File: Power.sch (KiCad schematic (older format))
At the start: 63 parts, among them J16 Power Input, J17 VS, J18 12V, J19 5V, J20 3.3V, Q8 YJS9435A, U6 MCP16301, U7 A4403, U8 MCP16301

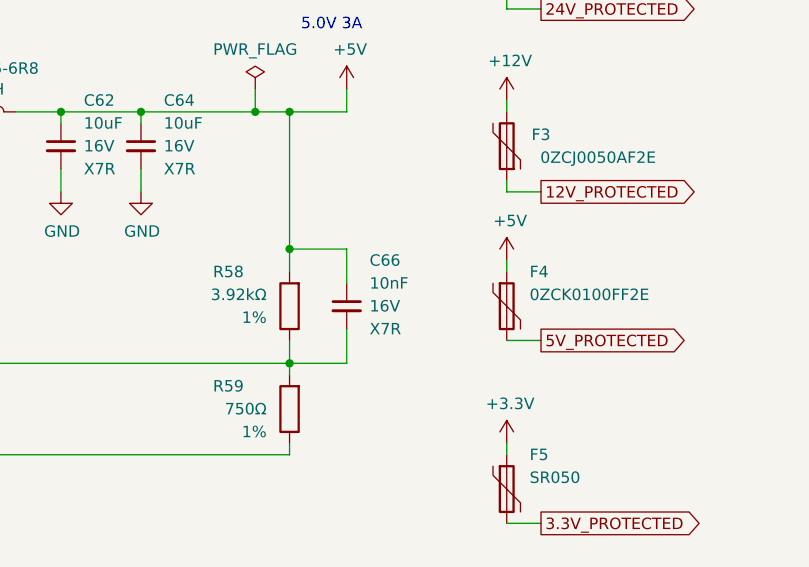
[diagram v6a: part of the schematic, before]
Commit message: Update elements value
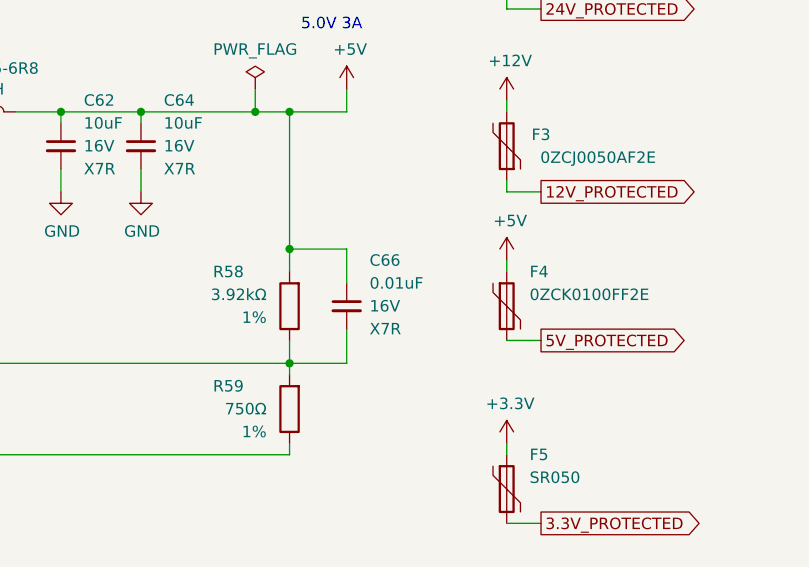
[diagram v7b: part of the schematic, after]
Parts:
- C66: value 10nF -> 0.01uF
- D24: Cena (none) -> 0.14862; Link (none) -> https://www.tme.eu/pl/details/mmsz5236bs-7-f/diody-zenera-s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; Model (none) -> MMSZ5236BS-7-F; Napięcie (none) -> 7.5V; Opis (none) -> Dioda: Zenera; 0,2W; 7,5V; SMD; rolka,taśma; SOD323; Producent (none) -> DIODES INCORPORATED; Typ (none) -> SMD
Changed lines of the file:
@@
 AR Path="/5E1018C2/5E102C60" Ref="C66"  Part="1"
 F 0 "C66" H 9000 3100 50  0000 L CNN
-F 1 "10nF" H 9000 3000 50  0000 L CNN
+F 1 "0.01uF" H 9000 3000 50  0000 L CNN
 F 2 "Capacitor_SMD:C_0603_1608Metric" H 8900 2900 50  0001 C CNN
 F 3 "~" H 8900 2900 50  0001 C CNN
@@
 F 2 "Diode_SMD:D_SOD-323" H 4750 6100 50  0001 C CNN
 F 3 "~" H 4750 6100 50  0001 C CNN
+F 4 "0.14862" H 4750 6100 50  0001 C CNN "Cena"
+F 5 "https://www.tme.eu/pl/details/mmsz5236bs-7-f/diody-zenera-smd/diodes-incorporated/" H 4750 6100 50  0001 C CNN "Link"
+F 6 "MMSZ5236BS-7-F" H 4750 6100 50  0001 C CNN "Model"
+F 7 "7.5V" H 4750 6100 50  0001 C CNN "Napięcie"
+F 8 "Dioda: Zenera; 0,2W; 7,5V; SMD; rolka,taśma; SOD323" H 4750 6100 50  0001 C CNN "Opis"
+F 9 "DIODES INCORPORATED" H 4750 6100 50  0001 C CNN "Producent"
+F 10 "SMD" H 4750 6100 50  0001 C CNN "Typ"
 	1    4750 6100
 	0    -1   -1   0

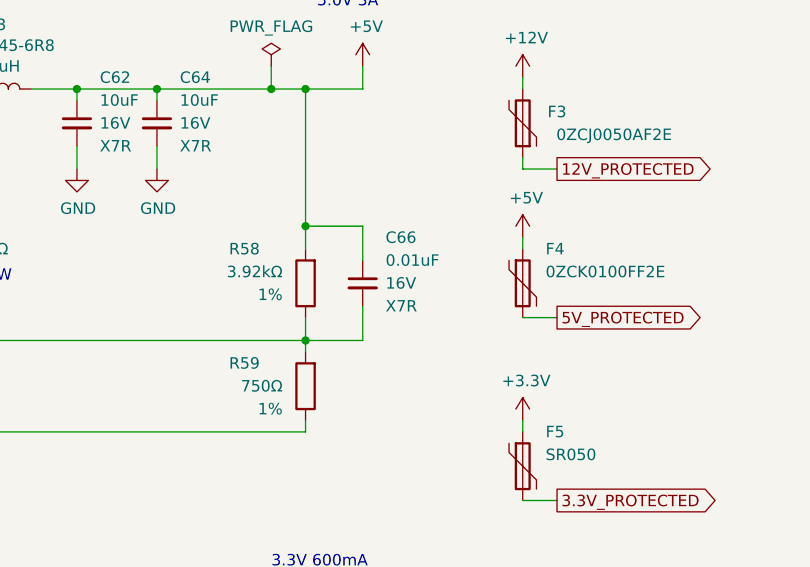
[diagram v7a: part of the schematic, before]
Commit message: Updated BOM on schematics
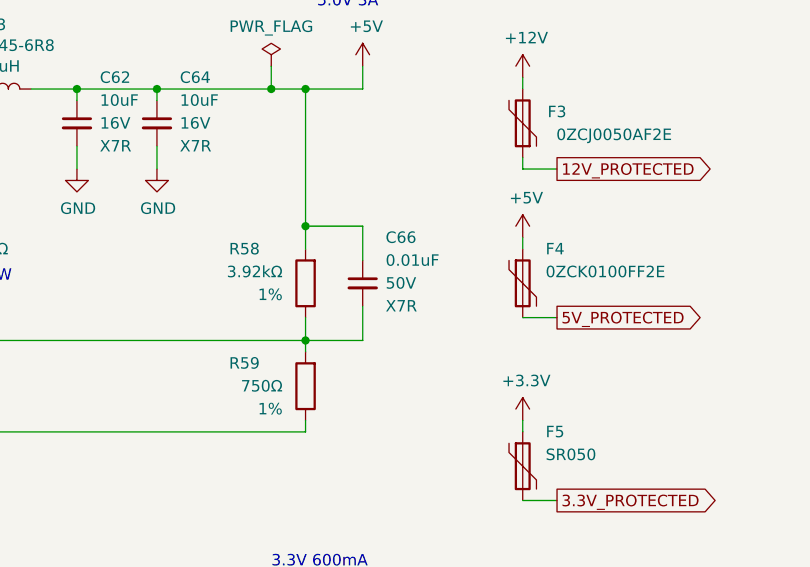
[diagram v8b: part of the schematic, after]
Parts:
- C49, C50, C52, C53, C54, C55: Opis (none) -> Kondensator: ceramiczny; MLCC; 2,2uF; 50V; X7R; ±10%; SMD; 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
- C51, C61: Cena 0.05982 -> 0.07894; Link (none) -> https://www.tme.eu/pl/details/cl10b104kb8nnnc/kondensatory-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; Model CL10B104KB8NNNC -> CL10B104KB8NNNC; Opis (none) -> Kondensator: ceramiczny; MLCC; 100nF; 50V; X7R; ±10%; SMD; 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
- C56: Cena (none) -> 0.06482; Link (none) -> https://www.tme.eu/pl/details/cl10b473kb8nnnc/kondensatory-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; Model (none) -> CL10B473KB8NNNC; Opis (none) -> Kondensator: ceramiczny; MLCC; 47nF; 50V; X7R; ±10%; SMD; 0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; Producent (none) -> SAMSUNG
- C57, C58, C62, C63, C64, C65: Link (none) -> https://www.tme.eu/pl/details/cl31b106kohnnne/kondensatory-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; Opis (none) -> Kondensator: ceramiczny; MLCC; 10uF; 16V; X7R; ±10%; SMD; 1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
- C59: Opis (none) -> Kondensator: ceramiczny; MLCC; 22nF; 50V; X7R; ±10%; SMD; 0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
- C66: Cena (none) -> 0.05269; Link (none) -> https://www.tme.eu/pl/details/vj0603y103kxacw1bc/kondensato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; Model (none) -> VJ0603Y103KXACW1BC; Napięcie 16V -> 50V; Opis (none) -> Kondensator: ceramiczny; MLCC; 10nF; 50V; X7R; ±10%; SMD; 0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; Producent (none) -> VISHAY
- L1: Link https://www.tme.eu/pl/details/djnr6045-150/dlawiki-smd-mocy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 -> https://www.tme.eu/pl/details/djnr6045-680/dlawiki-smd-mocy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; Model DJNR6045-150 -> DJNR6045-680; Opis Dławik: drutowy; SMD; 15uH; Ipracy: 2,3A; 100,1mΩ; 6x5,9x4,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 -> Dławik: drutowy; SMD; 68uH; Ipracy: 1A; 429mΩ; 6x5,9x4,5mm;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
- R45: Link (none) -> https://www.tme.eu/pl/details/crcw080510k0fktabc/rezystory-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
- R48, R52: Link (none) -> https://www.tme.eu/pl/details/smd0603-100k-1%25/rezystory-s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; Model (none) -> 0603SAF1003T5E; Opis (none) -> Rezystor: thick film; SMD; 0603; 100kΩ; 0,1W; ±1%; -55÷155°C; Producent (none) -> ROYAL OHM
- R53: Cena 0.04651 -> 0.03514; Link (none) -> https://www.tme.eu/pl/details/smd0603-47r-1%25/rezystory-sm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; Model (none) -> 0603SAF470JT5E; Opis (none) -> Rezystor: thick film; SMD; 0603; 47Ω; 0,1W; ±1%; -55÷155°C
- R59: Link (none) -> https://www.tme.eu/pl/details/smd0603-750r/rezystory-smd-06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; Model (none) -> 0603SAJ0751T5E; Opis (none) -> Rezystor: thick film; SMD; 0603; 750Ω; 0,1W; ±5%; -55÷155°C; Producent (none) -> ROYAL OHM
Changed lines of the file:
@@
 F 2 "Resistor_SMD:R_0603_1608Metric" V 6480 2350 50  0001 C CNN
 F 3 "~" H 6550 2350 50  0001 C CNN
-F 4 "" H 6550 2350 50  0001 C CNN "Model"
-F 5 "0.04651" H 6550 2350 50  0001 C CNN "Cena"
+F 4 "0603SAF470JT5E" H 6550 2350 50  0001 C CNN "Model"
+F 5 "0.03514" H 6550 2350 50  0001 C CNN "Cena"
 F 6 "SMD" H 6550 2350 50  0001 C CNN "Typ"
+F 7 "https://www.tme.eu/pl/details/smd0603-47r-1%25/rezystory-smd-0603/royal-ohm/0603saf470jt5e/" H 6550 2350 50  0001 C CNN "Link"
+F 8 "Rezystor: thick film; SMD; 0603; 47Ω; 0,1W; ±1%; -55÷155°C" H 6550 2350 50  0001 C CNN "Opis"
 	1    6550 2350
 	0    1    1    0
@@
 F 10 "10%" H 6250 1900 50  0001 C CNN "Tolerancja"
 F 11 "SMD" H 6250 1900 50  0001 C CNN "Typ"
+F 12 "Kondensator: ceramiczny; MLCC; 22nF; 50V; X7R; ±10%; SMD; 0603" H 6250 1900 50  0001 C CNN "Opis"
 	1    6250 1900
 	1    0    0    -1
@@
 F 9 "10%" H 7650 2200 50  0001 C CNN "Tolerancja"
 F 10 "SMD" H 7650 2200 50  0001 C CNN "Typ"
+F 11 "https://www.tme.eu/pl/details/cl31b106kohnnne/kondensatory-mlcc-smd-1206/samsung/" H 7650 2200 50  0001 C CNN "Link"
+F 12 "Kondensator: ceramiczny; MLCC; 10uF; 16V; X7R; ±10%; SMD; 1206" H 7650 2200 50  0001 C CNN "Opis"
 	1    7650 2200
 	1    0    0    -1
@@
 F 9 "10%" H 8000 2200 50  0001 C CNN "Tolerancja"
 F 10 "SMD" H 8000 2200 50  0001 C CNN "Typ"
+F 11 "https://www.tme.eu/pl/details/cl31b106kohnnne/kondensatory-mlcc-smd-1206/samsung/" H 8000 2200 50  0001 C CNN "Link"
+F 12 "Kondensator: ceramiczny; MLCC; 10uF; 16V; X7R; ±10%; SMD; 1206" H 8000 2200 50  0001 C CNN "Opis"
 	1    8000 2200
 	1    0    0    -1
@@
 F 2 "Capacitor_SMD:C_0603_1608Metric" H 8900 2900 50  0001 C CNN
 F 3 "~" H 8900 2900 50  0001 C CNN
-F 4 "16V" H 9000 2900 50  0000 L CNN "Napięcie"
+F 4 "50V" H 9000 2900 50  0000 L CNN "Napięcie"
 F 5 "X7R" H 9000 2800 50  0000 L CNN "Dielektryk"
 F 6 "SMD" H 8900 2900 50  0001 C CNN "Typ"
+F 7 "0.05269" H 8900 2900 50  0001 C CNN "Cena"
+F 8 "https://www.tme.eu/pl/details/vj0603y103kxacw1bc/kondensatory-mlcc-smd-0603/vishay/" H 8900 2900 50  0001 C CNN "Link"
+F 9 "VJ0603Y103KXACW1BC" H 8900 2900 50  0001 C CNN "Model"
+F 10 "Kondensator: ceramiczny; MLCC; 10nF; 50V; X7R; ±10%; SMD; 0603" H 8900 2900 50  0001 C CNN "Opis"
+F 11 "VISHAY" H 8900 2900 50  0001 C CNN "Producent"
 	1    8900 2900
 	1    0    0    -1
@@
 F 3 "~" H 8650 3350 50  0001 C CNN
 F 4 "1%" H 8750 3450 50  0000 L CNN "Tolerancja"
-F 5 "" H 8650 3350 50  0001 C CNN "Model"
+F 5 "0603SAJ0751T5E" H 8650 3350 50  0001 C CNN "Model"
 F 6 "0.04651" H 8650 3350 50  0001 C CNN "Cena"
 F 7 "SMD" H 8650 3350 50  0001 C CNN "Typ"
+F 8 "https://www.tme.eu/pl/details/smd0603-750r/rezystory-smd-0603/royal-ohm/0603saj0751t5e/" H 8650 3350 50  0001 C CNN "Link"
+F 9 "Rezystor: thick film; SMD; 0603; 750Ω; 0,1W; ±5%; -55÷155°C" H 8650 3350 50  0001 C CNN "Opis"
+F 10 "ROYAL OHM" H 8650 3350 50  0001 C CNN "Producent"
 	1    8650 3350
 	-1   0    0    1
@@
 F 5 "X7R" H 5100 3000 50  0000 L CNN "Dielektryk"
 F 6 "SMD" H 5000 3100 50  0001 C CNN "Typ"
+F 7 "0.06482" H 5000 3100 50  0001 C CNN "Cena"
+F 8 "https://www.tme.eu/pl/details/cl10b473kb8nnnc/kondensatory-mlcc-smd-0603/samsung/" H 5000 3100 50  0001 C CNN "Link"
+F 9 "CL10B473KB8NNNC" H 5000 3100 50  0001 C CNN "Model"
+F 10 "Kondensator: ceramiczny; MLCC; 47nF; 50V; X7R; ±10%; SMD; 0603" H 5000 3100 50  0001 C CNN "Opis"
+F 11 "SAMSUNG" H 5000 3100 50  0001 C CNN "Producent"
 	1    5000 3100
 	-1   0    0    1
@@
 F 2 "Resistor_SMD:R_0603_1608Metric" V 4930 1900 50  0001 C CNN
 F 3 "~" H 5000 1900 50  0001 C CNN
-F 4 "" H 5000 1900 50  0001 C CNN "Model"
+F 4 "0603SAF1003T5E" H 5000 1900 50  0001 C CNN "Model"
 F 5 "0.04651" H 5000 1900 50  0001 C CNN "Cena"
 F 6 "SMD" H 5000 1900 50  0001 C CNN "Typ"
+F 7 "https://www.tme.eu/pl/details/smd0603-100k-1%25/rezystory-smd-0603/royal-ohm/0603saf1003t5e/" H 5000 1900 50  0001 C CNN "Link"
+F 8 "Rezystor: thick film; SMD; 0603; 100kΩ; 0,1W; ±1%; -55÷155°C" H 5000 1900 50  0001 C CNN "Opis"
+F 9 "ROYAL OHM" H 5000 1900 50  0001 C CNN "Producent"
 	1    5000 1900
 	-1   0    0    1
@@
 F 9 "SAMSUNG" H 4600 1900 50  0001 C CNN "Producent"
 F 10 "SMD" H 4600 1900 50  0001 C CNN "Typ"
+F 11 "Kondensator: ceramiczny; MLCC; 2,2uF; 50V; X7R; ±10%; SMD; 1206" H 4600 1900 50  0001 C CNN "Opis"
 	1    4600 1900
 	1    0    0    -1
@@
 F 9 "SAMSUNG" H 4900 4500 50  0001 C CNN "Producent"
 F 10 "SMD" H 4900 4500 50  0001 C CNN "Typ"
+F 11 "Kondensator: ceramiczny; MLCC; 2,2uF; 50V; X7R; ±10%; SMD; 1206" H 4900 4500 50  0001 C CNN "Opis"
 	1    4900 4500
 	1    0    0    -1
@@
 F 4 "50V" H 6500 4250 50  0000 L CNN "Napięcie"
 F 5 "X7R" H 6500 4150 50  0000 L CNN "Dielektryk"
-F 6 "0.05982" H 6400 4250 50  0001 C CNN "Cena"
-F 7 "CL10B104KB8NNNC " H 6400 4250 50  0001 C CNN "Model"
+F 6 "0.07894" H 6400 4250 50  0001 C CNN "Cena"
+F 7 "CL10B104KB8NNNC" H 6400 4250 50  0001 C CNN "Model"
 F 8 "SAMSUNG" H 6400 4250 50  0001 C CNN "Producent"
 F 9 "10%" H 6400 4250 50  0001 C CNN "Tolerancja"
 F 10 "SMD" H 6400 4250 50  0001 C CNN "Typ"
+F 11 "https://www.tme.eu/pl/details/cl10b104kb8nnnc/kondensatory-mlcc-smd-0603/samsung/" H 6400 4250 50  0001 C CNN "Link"
+F 12 "Kondensator: ceramiczny; MLCC; 100nF; 50V; X7R; ±10%; SMD; 0603" H 6400 4250 50  0001 C CNN "Opis"
 	1    6400 4250
 	1    0    0    -1
@@
 F 9 "10%" H 7800 4600 50  0001 C CNN "Tolerancja"
 F 10 "SMD" H 7800 4600 50  0001 C CNN "Typ"
+F 11 "https://www.tme.eu/pl/details/cl31b106kohnnne/kondensatory-mlcc-smd-1206/samsung/" H 7800 4600 50  0001 C CNN "Link"
+F 12 "Kondensator: ceramiczny; MLCC; 10uF; 16V; X7R; ±10%; SMD; 1206" H 7800 4600 50  0001 C CNN "Opis"
 	1    7800 4600
 	1    0    0    -1
@@
 F 4 "0.04651" H 2700 2350 50  0001 C CNN "Cena"
 F 5 "SMD" H 2700 2350 50  0001 C CNN "Typ"
+F 6 "https://www.tme.eu/pl/details/smd0603-100k-1%25/rezystory-smd-0603/royal-ohm/0603saf1003t5e/" H 2700 2350 50  0001 C CNN "Link"
+F 7 "0603SAF1003T5E" H 2700 2350 50  0001 C CNN "Model"
+F 8 "Rezystor: thick film; SMD; 0603; 100kΩ; 0,1W; ±1%; -55÷155°C" H 2700 2350 50  0001 C CNN "Opis"
+F 9 "ROYAL OHM" H 2700 2350 50  0001 C CNN "Producent"
 	1    2700 2350
 	1    0    0    -1
@@
 F 9 "SAMSUNG" H 2350 6450 50  0001 C CNN "Producent"
 F 10 "SMD" H 2350 6450 50  0001 C CNN "Typ"
+F 11 "Kondensator: ceramiczny; MLCC; 2,2uF; 50V; X7R; ±10%; SMD; 1206" H 2350 6450 50  0001 C CNN "Opis"
 	1    2350 6450
 	1    0    0    -1
@@
 F 4 "68uH" V 4400 6400 50  0000 C CNN "Induktancja"
 F 5 "0.7018" H 4300 6400 50  0001 C CNN "Cena"
-F 6 "https://www.tme.eu/pl/details/djnr6045-150/dlawiki-smd-mocy/ferrocore/" H 4300 6400 50  0001 C CNN "Link"
-F 7 "DJNR6045-150" H 4300 6400 50  0001 C CNN "Model"
-F 8 "Dławik: drutowy; SMD; 15uH; Ipracy: 2,3A; 100,1mΩ; 6x5,9x4,5mm; ±20%" H 4300 6400 50  0001 C CNN "Opis"
+F 6 "https://www.tme.eu/pl/details/djnr6045-680/dlawiki-smd-mocy/ferrocore/" H 4300 6400 50  0001 C CNN "Link"
+F 7 "DJNR6045-680" H 4300 6400 50  0001 C CNN "Model"
+F 8 "Dławik: drutowy; SMD; 68uH; Ipracy: 1A; 429mΩ; 6x5,9x4,5mm; ±20%" H 4300 6400 50  0001 C CNN "Opis"
 F 9 "FERROCORE" H 4300 6400 50  0001 C CNN "Producent"
 F 10 "SMD" H 4300 6400 50  0001 C CNN "Typ"
@@
 F 4 "50V" H 3950 6200 50  0000 L CNN "Napięcie"
 F 5 "X7R" H 3950 6100 50  0000 L CNN "Dielektryk"
-F 6 "0.05982" H 3850 6200 50  0001 C CNN "Cena"
-F 7 "CL10B104KB8NNNC " H 3850 6200 50  0001 C CNN "Model"
+F 6 "0.07894" H 3850 6200 50  0001 C CNN "Cena"
+F 7 "CL10B104KB8NNNC" H 3850 6200 50  0001 C CNN "Model"
 F 8 "SAMSUNG" H 3850 6200 50  0001 C CNN "Producent"
 F 9 "10%" H 3850 6200 50  0001 C CNN "Tolerancja"
 F 10 "SMD" H 3850 6200 50  0001 C CNN "Typ"
+F 11 "https://www.tme.eu/pl/details/cl10b104kb8nnnc/kondensatory-mlcc-smd-0603/samsung/" H 3850 6200 50  0001 C CNN "Link"
+F 12 "Kondensator: ceramiczny; MLCC; 100nF; 50V; X7R; ±10%; SMD; 0603" H 3850 6200 50  0001 C CNN "Opis"
 	1    3850 6200
 	1    0    0    -1
@@
 F 9 "10%" H 5250 6550 50  0001 C CNN "Tolerancja"
 F 10 "SMD" H 5250 6550 50  0001 C CNN "Typ"
+F 11 "https://www.tme.eu/pl/details/cl31b106kohnnne/kondensatory-mlcc-smd-1206/samsung/" H 5250 6550 50  0001 C CNN "Link"
+F 12 "Kondensator: ceramiczny; MLCC; 10uF; 16V; X7R; ±10%; SMD; 1206" H 5250 6550 50  0001 C CNN "Opis"
 	1    5250 6550
 	1    0    0    -1
@@
 F 9 "10%" H 5600 6550 50  0001 C CNN "Tolerancja"
 F 10 "SMD" H 5600 6550 50  0001 C CNN "Typ"
+F 11 "https://www.tme.eu/pl/details/cl31b106kohnnne/kondensatory-mlcc-smd-1206/samsung/" H 5600 6550 50  0001 C CNN "Link"
+F 12 "Kondensator: ceramiczny; MLCC; 10uF; 16V; X7R; ±10%; SMD; 1206" H 5600 6550 50  0001 C CNN "Opis"
 	1    5600 6550
 	1    0    0    -1
@@
 F 9 "SAMSUNG" H 4200 1900 50  0001 C CNN "Producent"
 F 10 "SMD" H 4200 1900 50  0001 C CNN "Typ"
+F 11 "Kondensator: ceramiczny; MLCC; 2,2uF; 50V; X7R; ±10%; SMD; 1206" H 4200 1900 50  0001 C CNN "Opis"
 	1    4200 1900
 	1    0    0    -1
@@
 F 9 "SAMSUNG" H 4500 4500 50  0001 C CNN "Producent"
 F 10 "SMD" H 4500 4500 50  0001 C CNN "Typ"
+F 11 "Kondensator: ceramiczny; MLCC; 2,2uF; 50V; X7R; ±10%; SMD; 1206" H 4500 4500 50  0001 C CNN "Opis"
 	1    4500 4500
 	1    0    0    -1
@@
 F 9 "SAMSUNG" H 1950 6450 50  0001 C CNN "Producent"
 F 10 "SMD" H 1950 6450 50  0001 C CNN "Typ"
+F 11 "Kondensator: ceramiczny; MLCC; 2,2uF; 50V; X7R; ±10%; SMD; 1206" H 1950 6450 50  0001 C CNN "Opis"
 	1    1950 6450
 	1    0    0    -1
@@
 F 9 "10%" H 8150 4600 50  0001 C CNN "Tolerancja"
 F 10 "SMD" H 8150 4600 50  0001 C CNN "Typ"
+F 11 "https://www.tme.eu/pl/details/cl31b106kohnnne/kondensatory-mlcc-smd-1206/samsung/" H 8150 4600 50  0001 C CNN "Link"
+F 12 "Kondensator: ceramiczny; MLCC; 10uF; 16V; X7R; ±10%; SMD; 1206" H 8150 4600 50  0001 C CNN "Opis"
 	1    8150 4600
 	1    0    0    -1
@@
 F 4 "0.04651" H 1400 4150 50  0001 C CNN "Cena"
 F 5 "SMD" H 1400 4150 50  0001 C CNN "Typ"
+F 6 "https://www.tme.eu/pl/details/crcw080510k0fktabc/rezystory-smd-0805/vishay/" H 1400 4150 50  0001 C CNN "Link"
 	1    1400 4150
 	1    0    0    -1
